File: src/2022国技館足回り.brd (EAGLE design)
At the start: 13 parts

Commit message: 国技館足回り回路の追加
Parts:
- removed MAT_LED: 02-JST, con-jst-xh:B2B-XH
- added C1: 100nF, rcl:C025-024X044
- added LED1, LED2, LED3, LED4, LED5, LED6: (no value), led:LED5MM
- added POW: 02-JST, con-jst-xh:B2B-XH
- added R1, R2, R3, R4, R5, R6: 100, rcl:0204/7
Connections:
- new net BUSY: JP1.38, JP8.1
- new net LED1: JP2.22, R2.1
- new net LED2: JP2.24, R3.1
- new net LED3: JP2.26, R4.1
- new net LED4: JP2.28, R5.1
- new net LED5: JP2.30, R6.1
- new net N$1: LED3.A, R3.2
- new net N$2: LED2.A, R2.2
- new net N$3: LED1.A, R1.2
- new net N$5: LED6.A, R6.2
- new net N$6: LED5.A, R5.2
- new net N$7: LED4.A, R4.2
- new net RESET: JP1.32, JP8.8
- new net SLEEP: JP1.30, JP9.2
- new net STATUS: JP1.34, JP8.6
- new net VIN: C1.1, JP1.24, POW.2, R1.1
- new net XMIT: JP1.36, JP8.2
- net 3V3: now also JP1.16, JP8.7
- net 5V: now also JP1.18
- net ENC1_A: now also JP1.15
- net ENC1_B: now also JP1.13
- net ENC2_A: now also JP1.27
- net ENC2_B: now also JP1.25
- net ENC3_A: now also JP1.31
- net ENC3_B: now also JP1.29
- net ENC4_A: now also JP1.37
- net ENC4_B: now also JP1.35
- net GND: now also C1.2, JP1.20, JP9.8, LED1.K, LED2.K, LED3.K, LED4.K, LED5.K, LED6.K, POW.1
- net RX1: now also JP1.21, JP8.4; no longer MAT_LED.1
- net SCL: now also JP2.3
- net SDA: now also JP2.5
- net TX1: now also JP1.17, JP9.3; no longer MAT_LED.2

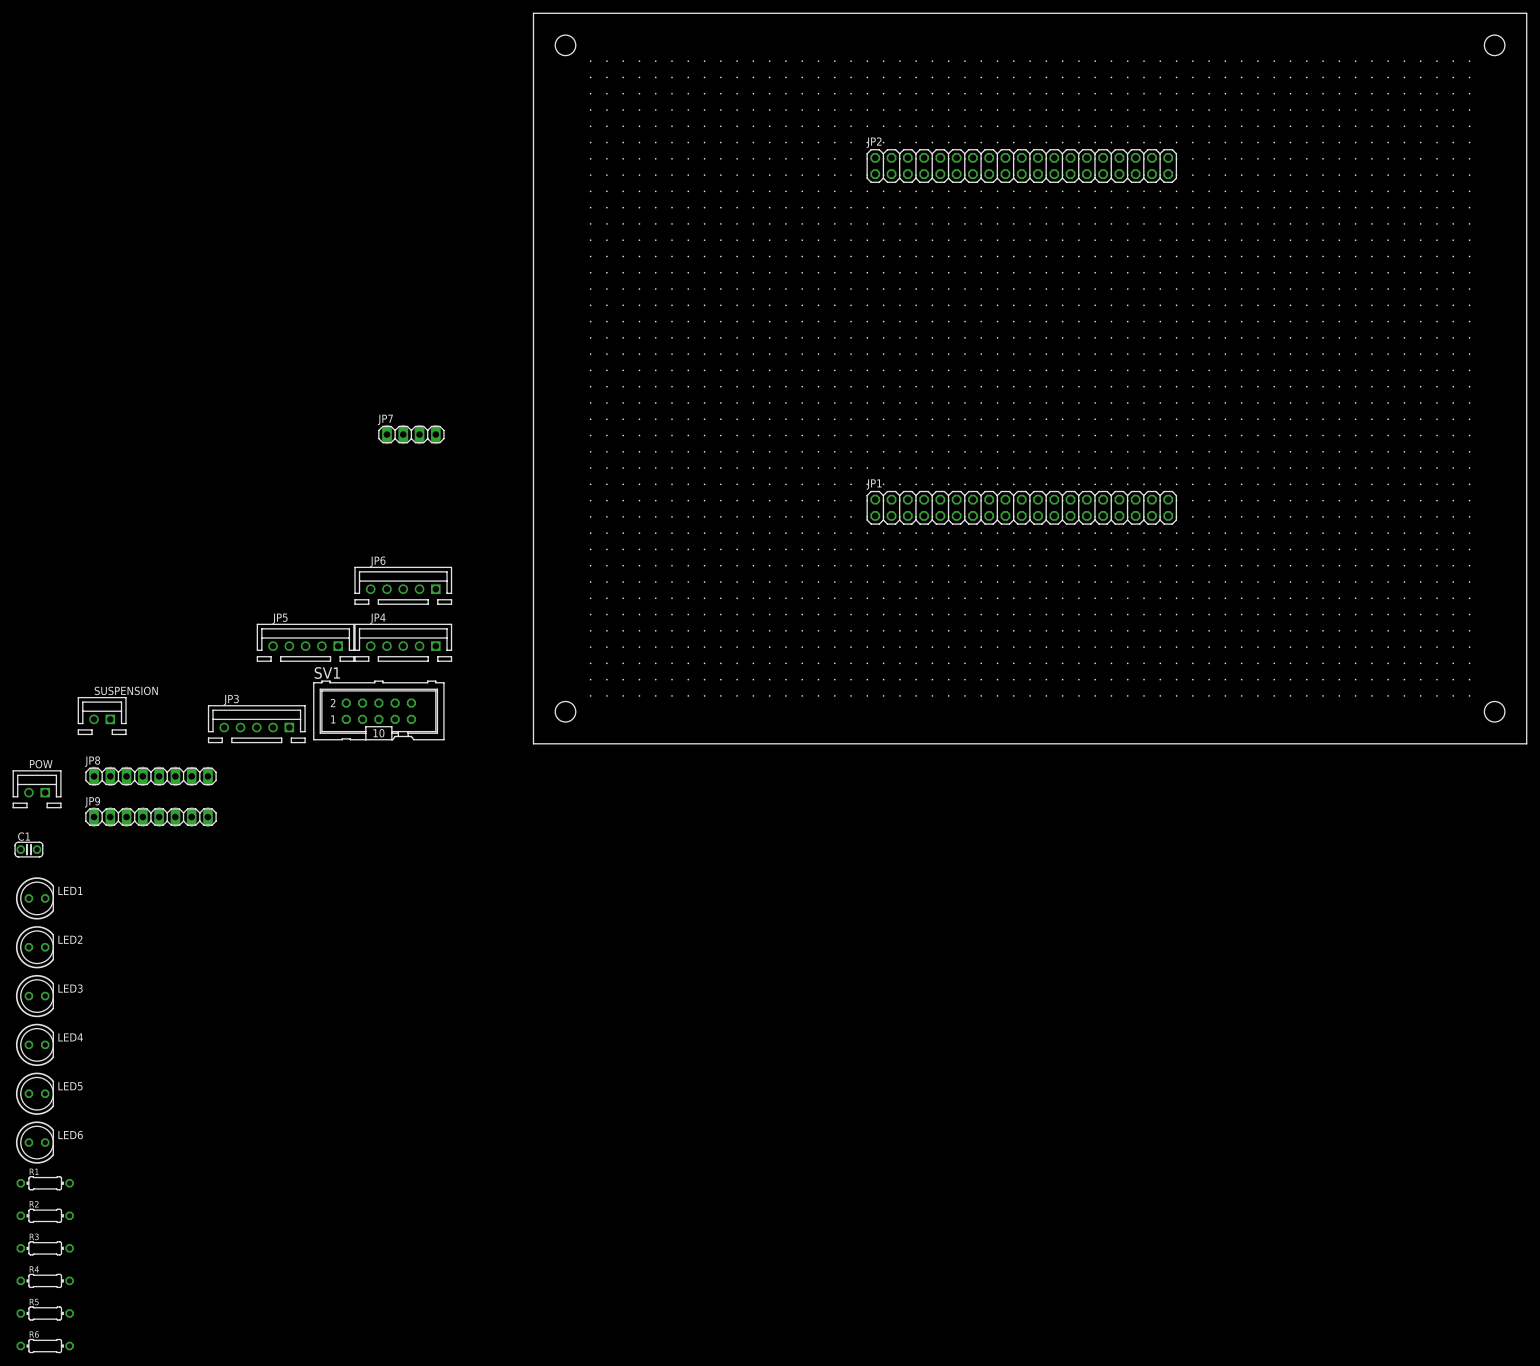
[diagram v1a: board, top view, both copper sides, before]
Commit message: 足回りコントローラ
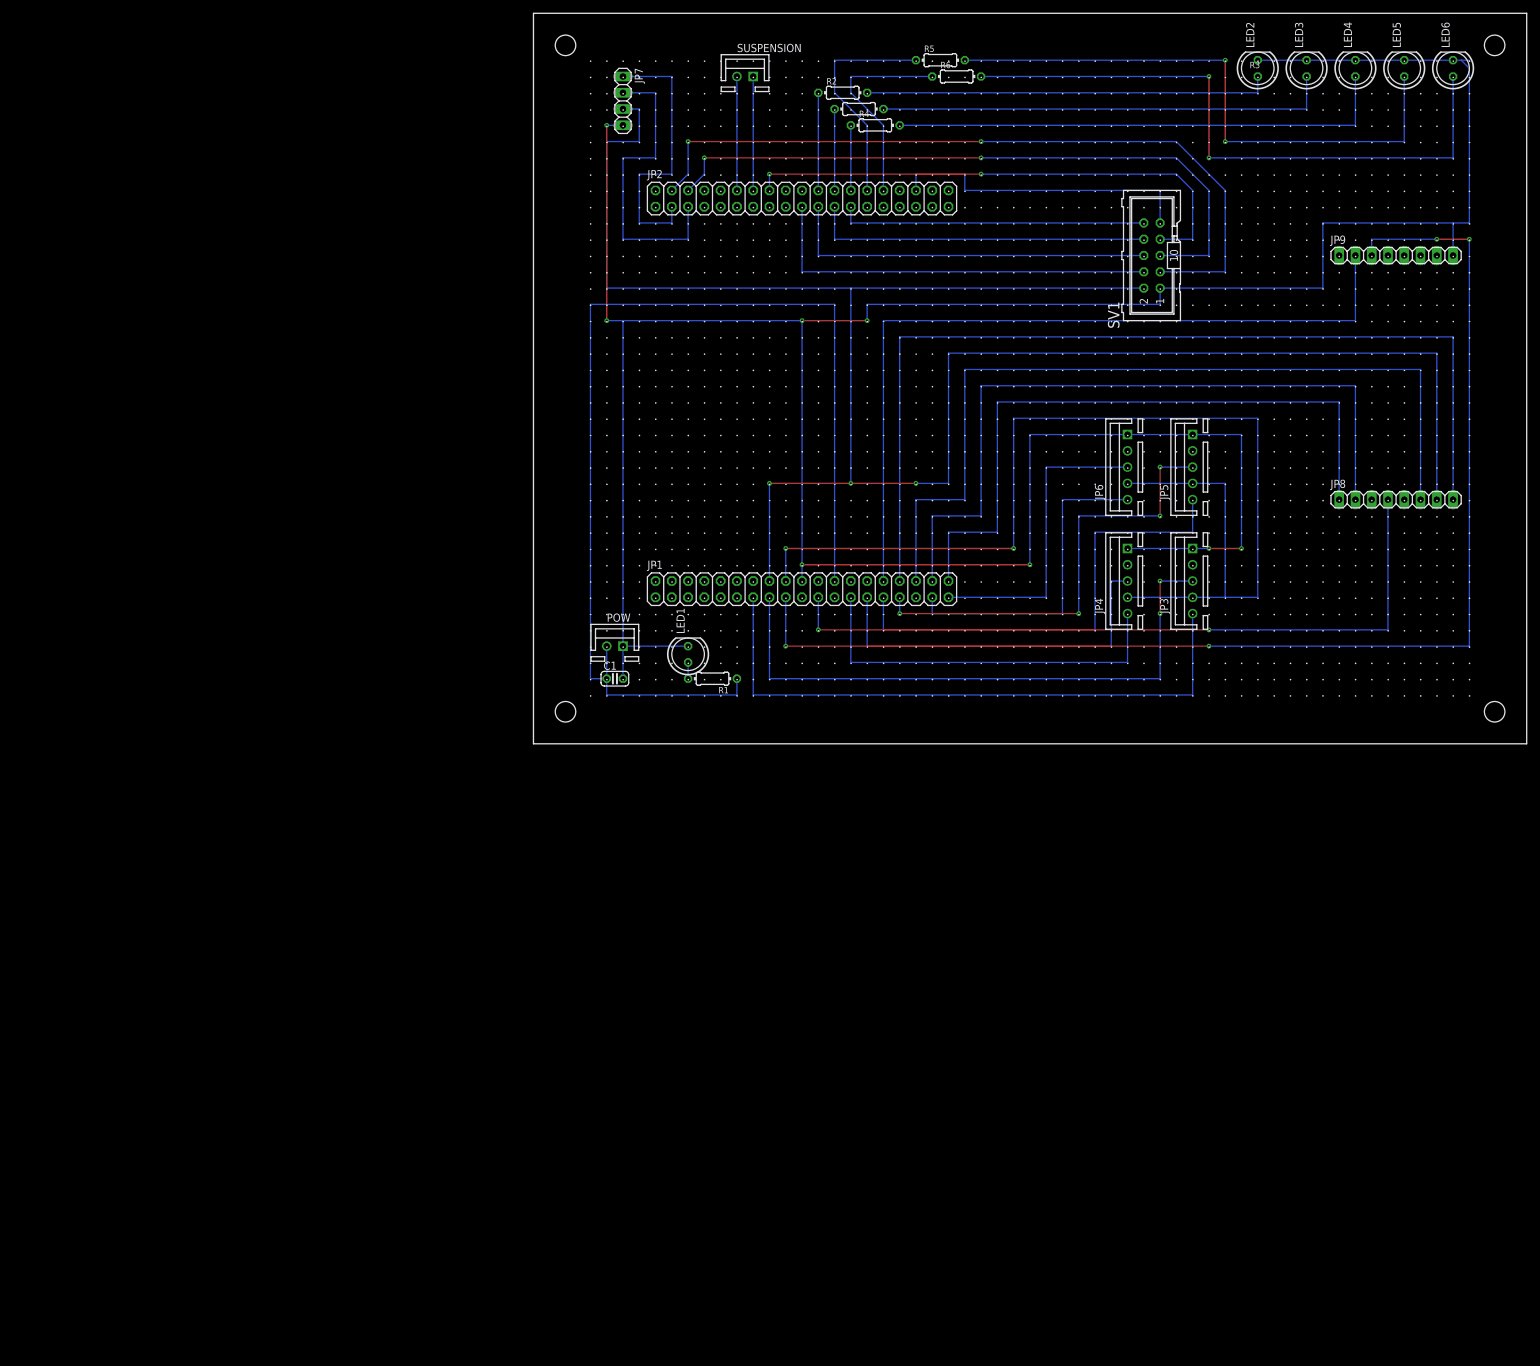
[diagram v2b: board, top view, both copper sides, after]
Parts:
- moved LED6 277.4 mm to (143.5, 105.4), turned to 90 degrees
- moved LED5 266.7 mm to (135.9, 105.4), turned to 90 degrees
- moved LED4 256.0 mm to (128.3, 105.4), turned to 90 degrees
- moved LED3 245.4 mm to (120.7, 105.4), turned to 90 degrees
- moved R6 243.9 mm to (66.0, 104.1)
- moved R5 240.3 mm to (63.5, 106.7)
- moved LED2 234.7 mm to (113.0, 105.4), turned to 90 degrees
- moved R4 222.0 mm to (53.3, 96.5)
- moved R3 218.5 mm to (50.8, 99.1)
- moved R2 215.0 mm to (48.3, 101.6)
- moved JP9 213.2 mm to (134.6, 76.2)
- moved JP8 199.0 mm to (134.6, 38.1)
- moved JP3 147.8 mm to (102.9, 25.4), turned to 90 degrees
- moved SUSPENSION 141.9 mm to (33.0, 104.1)
- moved JP5 141.2 mm to (102.9, 43.2), turned to 90 degrees
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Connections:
- net DIR1: now also JP2.34; no longer JP2.25
- net DIR2: now also JP2.16; no longer JP2.23
- net DIR3: now also JP2.6; no longer JP2.21
- net DIR4: now also JP2.4; no longer JP2.19
- net PWM1: now also JP2.25; no longer JP2.27
- net PWM2: now also JP2.23; no longer JP2.29
- net PWM3: now also JP2.21; no longer JP2.31
- net PWM4: now also JP2.19; no longer JP2.33
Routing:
- net GND: track 0.00 -> 478.0 mm, vias 0 -> 8
- net 3V3: track 0.00 -> 312.4 mm, vias 0 -> 3
- net TX1: track 0.00 -> 195.6 mm, vias 0 -> 4
- net 5V: track 0.00 -> 180.3 mm, vias 0 -> 2
- net VIN: track 0.00 -> 172.7 mm
- net RESET: track 0.00 -> 149.9 mm
- net STATUS: track 0.00 -> 132.1 mm
- net SLEEP: track 0.00 -> 124.5 mm
- net DIR4: track 0.00 -> 118.5 mm, vias 0 -> 2
- net XMIT: track 0.00 -> 114.3 mm
- net RX1: track 0.00 -> 114.3 mm, vias 0 -> 2
- net DIR3: track 0.00 -> 104.8 mm, vias 0 -> 2
- net BUSY: track 0.00 -> 104.1 mm
- net N$5: track 0.00 -> 99.1 mm, vias 0 -> 2
- net ENC1_B: track 0.00 -> 96.5 mm
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
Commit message: 国技館足回り修正前
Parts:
- removed JP7: (no value), pinhead:1X04
- added REMOTE_SW: 02-JST, con-jst-xh:B2B-XH
- moved LED1 2.54 mm to (21.6, 14.0)
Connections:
- removed net SCL: JP2.3, JP7.1
- removed net SDA: JP2.5, JP7.2
- new net EMERGENCY: JP2.2, REMOTE_SW.2
- net 3V3: no longer JP7.3
- net ENC2_A: now also JP1.1; no longer JP1.27
- net ENC2_B: now also JP1.3; no longer JP1.25
- net ENC3_A: now also JP2.5; no longer JP1.31
- net ENC3_B: now also JP2.3; no longer JP1.29
- net GND: now also REMOTE_SW.1; no longer JP7.4
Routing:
- net 3V3: track 312.4 -> 238.8 mm
- net ENC3_A: track 71.1 -> 139.7 mm, vias 4 -> 8
- net ENC3_B: track 73.7 -> 132.1 mm, vias 0 -> 4
- net SDA: track 48.3 -> 0.00 mm
- net SCL: track 43.2 -> 0.00 mm
- net ENC2_A: track 58.4 -> 91.4 mm, vias 0 -> 2
- net ENC2_B: track 61.0 -> 88.9 mm, vias 0 -> 2
- net EMERGENCY: track 0.00 -> 17.8 mm
- net GND: track 478.0 -> 483.1 mm
- net DIR3: track 104.8 -> 106.2 mm
- net DIR4: track 118.5 -> 120.0 mm
- net N$3: track 2.54 -> 3.59 mm

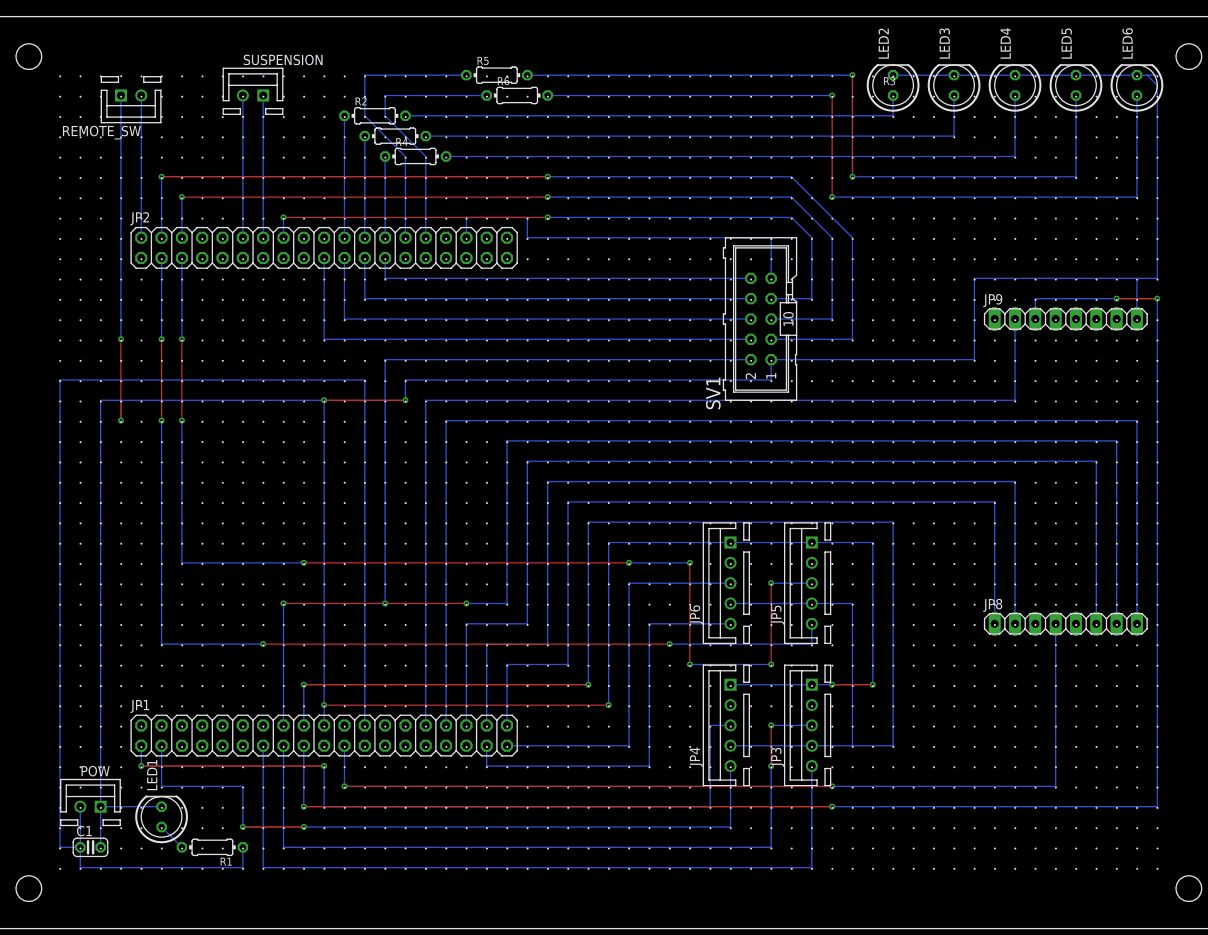
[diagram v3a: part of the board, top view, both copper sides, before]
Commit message: 国技館足回り修正後
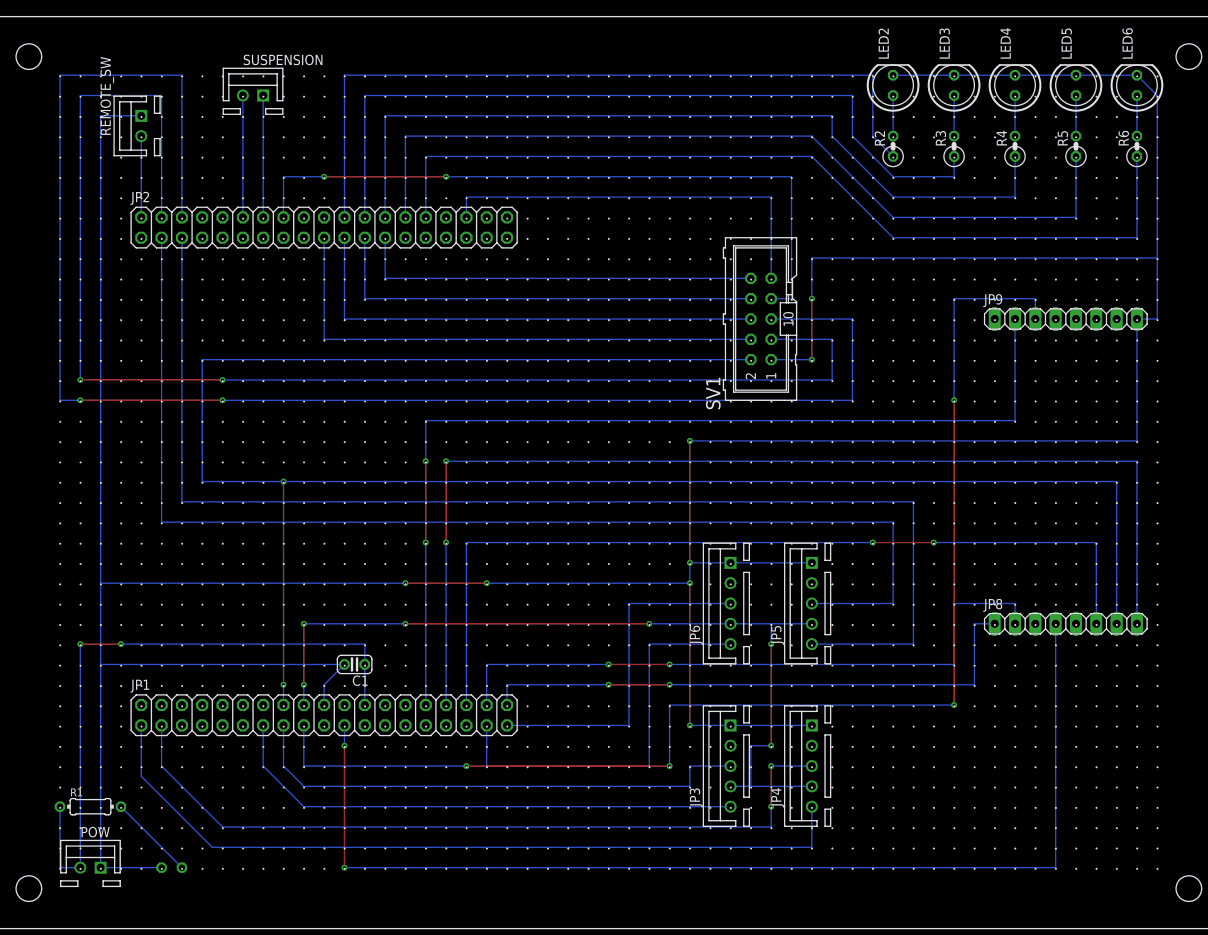
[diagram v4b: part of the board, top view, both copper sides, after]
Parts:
- R2, R3, R4, R5, R6: device rcl:0204/7 -> rcl:0207/2V
- moved R6 77.7 mm to (143.5, 97.8), turned to 90 degrees
- moved R4 74.9 mm to (128.3, 97.8), turned to 90 degrees
- moved R5 72.9 mm to (135.9, 97.8), turned to 90 degrees
- moved R3 69.9 mm to (120.7, 97.8), turned to 90 degrees
- moved R2 64.9 mm to (113.0, 97.8), turned to 90 degrees
- moved C1 40.2 mm to (45.7, 33.0), turned to 180 degrees
- moved R1 16.1 mm to (12.7, 15.2), turned to 0 degrees
- moved JP3 11.4 mm to (92.7, 20.3)
- moved JP4 11.4 mm to (102.9, 20.3)
- moved POW 7.62 mm to (12.7, 7.62)
- moved LED1 6.48 mm to (22.9, 7.62), flipped to the bottom, turned to 0 degrees
- moved REMOTE_SW 4.02 mm to (19.1, 100.3), turned to 90 degrees
- moved JP1 2.54 mm to (41.9, 26.7)
- moved JP5 2.54 mm to (102.9, 40.6)
- moved JP6 2.54 mm to (92.7, 40.6)
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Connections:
- net ENC2_A: now also JP1.3; no longer JP1.1
- net ENC2_B: now also JP1.1; no longer JP1.3
- net ENC3_A: now also JP2.3; no longer JP2.5
- net ENC3_B: now also JP2.5; no longer JP2.3
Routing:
- net N$5: track 99.1 -> 5.08 mm, vias 2 -> 0
- net LED3: track 10.2 -> 102.2 mm
- net VIN: track 172.7 -> 81.3 mm, vias 0 -> 2
- net DIR3: track 106.2 -> 193.0 mm
- net N$6: track 91.4 -> 5.08 mm, vias 2 -> 0
- net LED2: track 12.7 -> 98.6 mm
- net LED1: track 15.2 -> 95.0 mm
- net LED5: track 32.6 -> 110.9 mm
- net N$7: track 78.7 -> 5.08 mm
- net 5V: track 180.3 -> 106.7 mm, vias 2 -> 6
- net LED4: track 35.1 -> 105.8 mm
- net N$1: track 71.1 -> 5.08 mm
- net N$2: track 63.5 -> 5.08 mm
- net DIR4: track 120.0 -> 167.6 mm
- net TX1: track 195.6 -> 157.5 mm
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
